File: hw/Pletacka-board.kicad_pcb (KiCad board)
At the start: 2 copper layers, 29.7 x 86.9 mm, 37 parts, among them J4 STOP_INPUT, J5 POWER_&_FINN_INPUT, SW1 Reset_Button, SW2 User_Button, U1 TPS54231D, U2 EL357N(A)(TA)-G, U3 EL357N(A)(TA)-G

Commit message: Add Kuba Logo
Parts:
- added G***: LOGO, Logos:Kuba-logo, F.Cu at (146.6, 108.7)

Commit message: Fix small issues
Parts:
- moved C6 11.5 mm to (152.1, 111.5), turned to 180 degrees
- moved C5 6.43 mm to (148.8, 125.7), turned to 0 degrees
- moved L1 1.85 mm to (152.9, 117.6)
- moved D5 1.78 mm to (150.9, 123.4)
- moved R4 0.80 mm to (157.2, 124.5)
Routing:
- net Net-(C5-Pad1): track 13.6 -> 1.94 mm, vias 2 -> 0
- net Net-(C5-Pad2): track 0.00 -> 3.02 mm
- net +3V3: track 71.8 -> 74.8 mm
- net GND: vias 5 -> 9

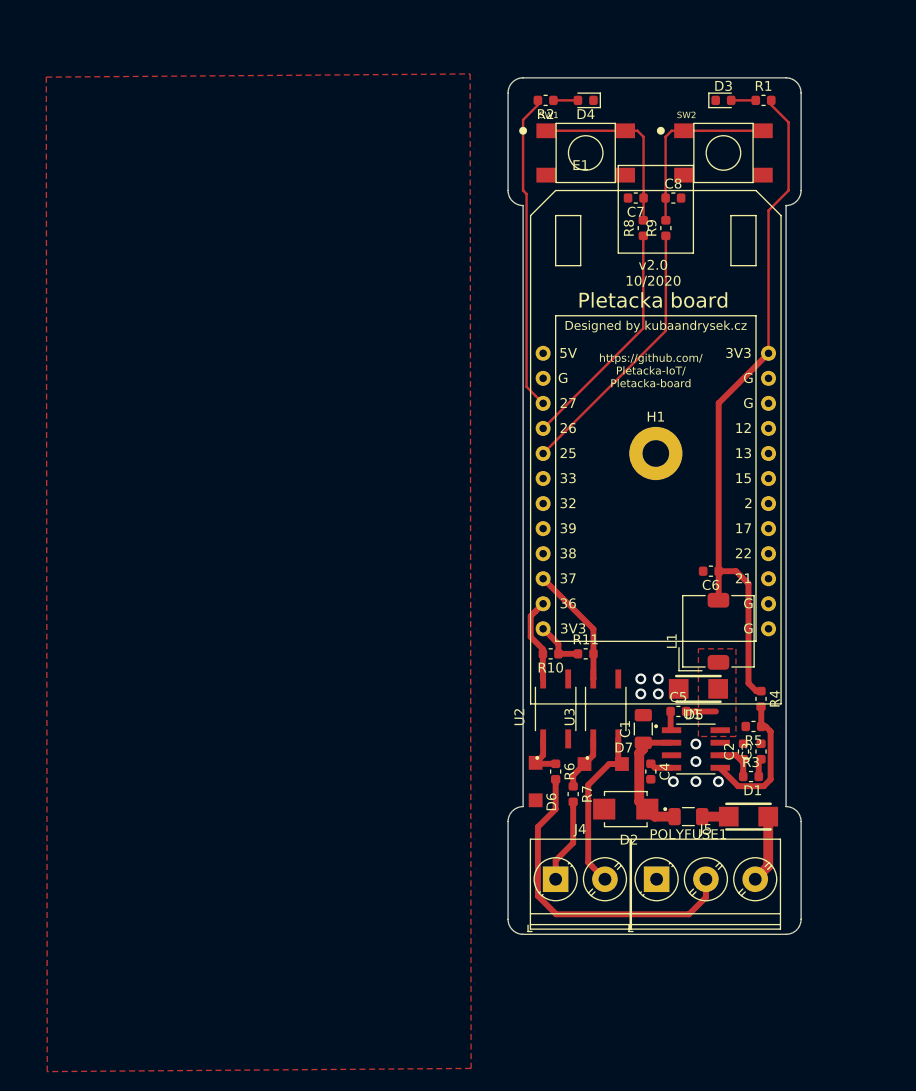
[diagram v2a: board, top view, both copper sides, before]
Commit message: Change Inductor
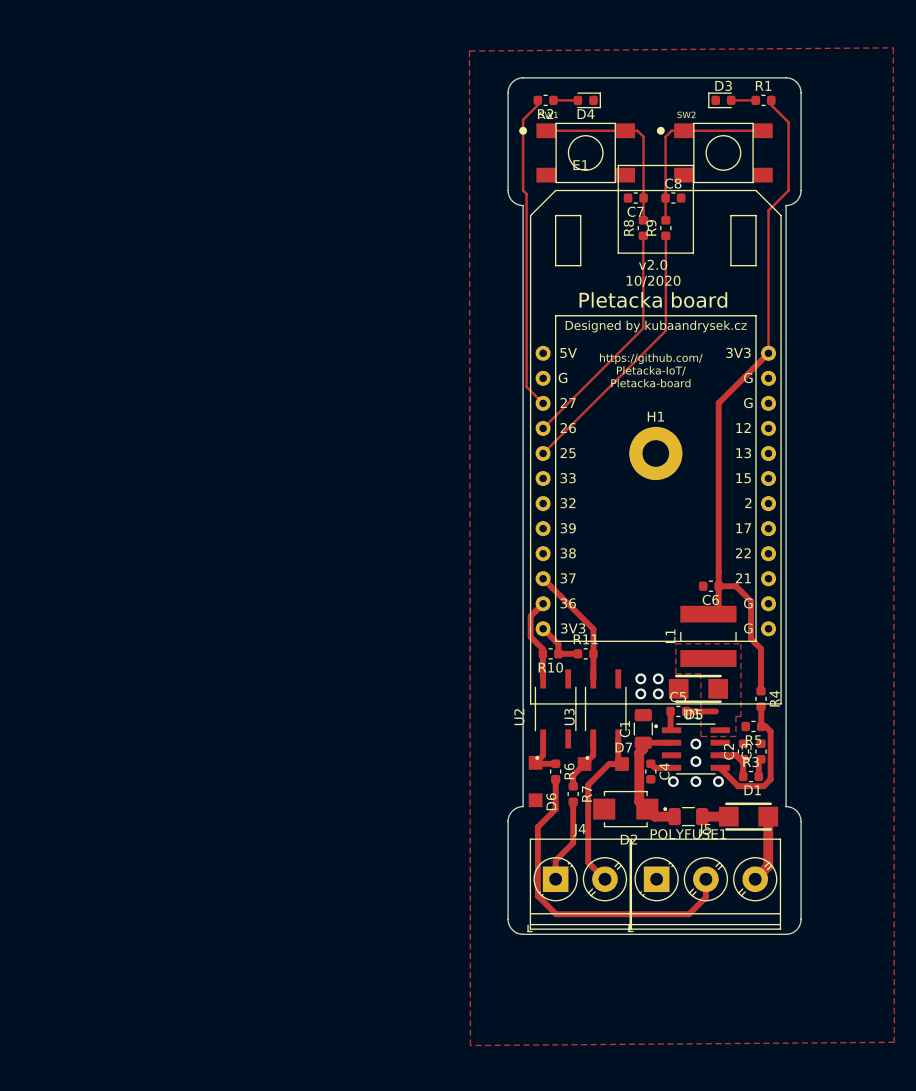
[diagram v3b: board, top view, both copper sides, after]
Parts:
- L1: footprint Inductor_SMD:L_TDK_SLF7045 -> SLW6045S220MST:SLW
- moved C6 1.52 mm to (152.1, 113.0)
- moved L1 1.14 mm to (151.9, 118.1)

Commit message: Finish board
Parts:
- added JP1: Jumper_NO_Small, Jumper:SolderJumper-2_P1.3mm_Open_Pad1.0x1.5mm, B.Cu at (140.5, 106.7)
- added JP2: Jumper, Jumper:SolderJumper-2_P1.3mm_Bridged_Pad1.0x1.5mm, F.Cu at (152.9, 101.9)
- added Pins1: Pins, Connector_PinHeader_2.54mm:PinHeader_1x05_P2.54mm_Vertical, F.Cu at (141.2, 63.0)
- moved C5 6.36 mm to (155.2, 125.5), turned to 180 degrees
- moved R4 2.83 mm to (157.5, 121.6)
- moved D4 2.03 mm to (137.4, 63.8)
- moved R7 2.03 mm to (138.2, 136.1)
- moved D3 1.78 mm to (155.2, 63.8)
- moved R2 1.75 mm to (133.6, 63.8)
- moved R1 1.52 mm to (159.0, 63.8)
- moved R6 1.14 mm to (136.9, 132.8)
- moved R8 0.57 mm to (144.8, 76.5)
- moved C7 0.51 mm to (144.0, 73.7)
- moved D6 0.51 mm to (134.9, 132.8)
- moved R9 0.36 mm to (147.8, 76.5)
- moved C8 0.25 mm to (148.6, 73.7)
- renumbered E1 to ESP1, H1 to MHole1, J5 to POWER_&_FINN_INPUT1, J4 to STOP_INPUT1
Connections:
- C6 pad 1: +3V3 -> Net-(C6-Pad1)
- ESP1 pad 25: BTN_USER -> USER_IO25
- ESP1 pad 32: Net-(E1-Pad32) -> BTN_USER
- ESP1 pad 33: Net-(E1-Pad33) -> USER_IO33
- L1 pad 2: +3V3 -> Net-(C6-Pad1)
- R4 pad 1: +3V3 -> Net-(C6-Pad1)
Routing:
- net +5V: track 0.00 -> 52.3 mm
- net USER_IO33: track 0.00 -> 44.8 mm
- net USER_IO25: track 0.00 -> 42.0 mm
- net Net-(C1-Pad1): track 13.0 -> 41.5 mm, vias 0 -> 1
- net Net-(C6-Pad1): track 0.00 -> 24.2 mm
- net +3V3: track 74.6 -> 53.8 mm
- net Net-(C5-Pad1): track 1.94 -> 12.7 mm, vias 0 -> 2
- net BTN_USER: track 27.2 -> 32.7 mm
- net Net-(R4-Pad2): track 14.2 -> 17.8 mm
- net OPTO_FINISHED_IN_PLUS: track 32.9 -> 29.6 mm
- net Net-(C5-Pad2): track 3.02 -> 0.00 mm
- net Net-(C7-Pad1): track 18.6 -> 16.5 mm
- net Net-(D7-PadC): track 5.65 -> 7.68 mm
- net OPTO_STOP_IN_PLUS: track 8.58 -> 6.55 mm
- net Net-(C8-Pad1): track 18.6 -> 17.5 mm
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- added copper zone on B.Cu, net GND
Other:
- board size 29.7 x 86.9 mm -> 29.7 x 87.4 mm
- board text added: "3V 33 25 5V"
- board text added: "5V 25 33 3V"
- board text added: "FIN"
- board text added: "G"
- board text added: "PWR"
- board text added: "RESET"
- board text added: "STP"
- board text added: "USER BTN"
- board text added: "VCC"
- board text added: "VCC->5V"
- board text removed: "v2.0 10/2020"
